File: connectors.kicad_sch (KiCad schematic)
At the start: 14 parts, among them J1 USB-C_DX07S024JJ2, J2 PCIe_x4_Conn_EdgeMount_NoMill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, J3 Molex_Nano-Fit-1053xx_xx02-ho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

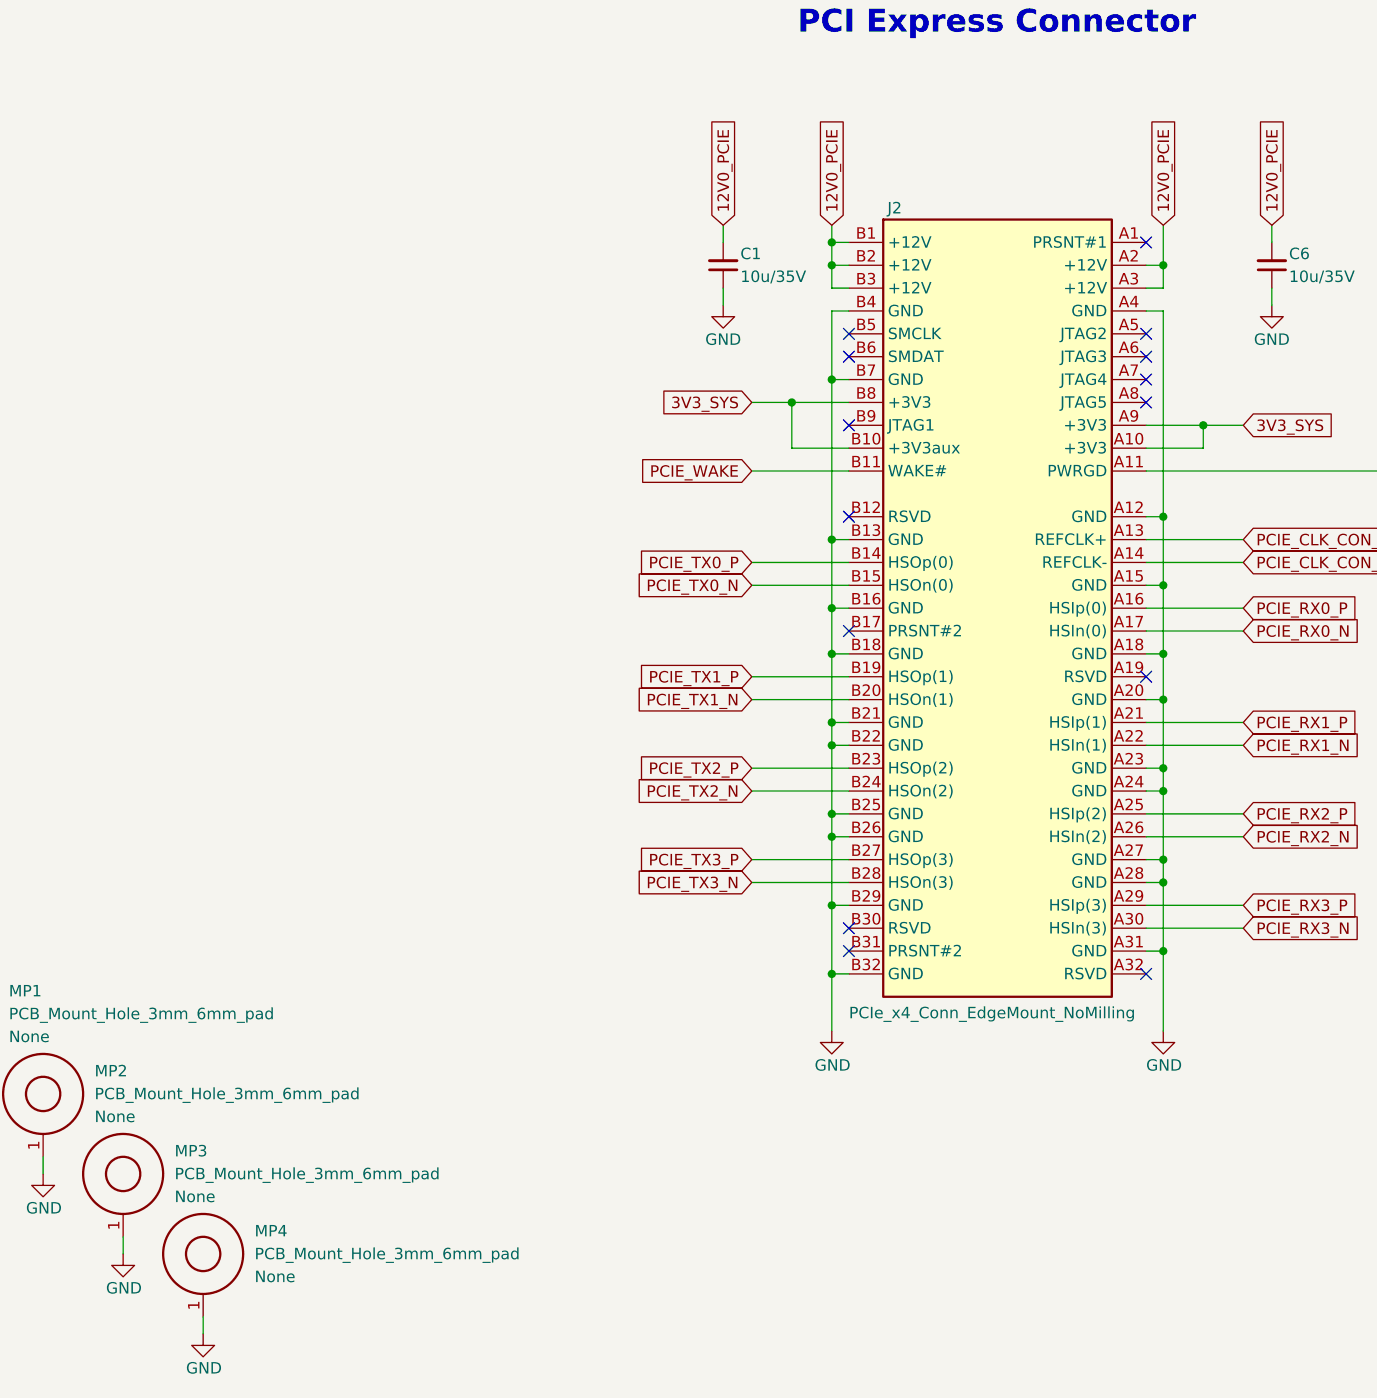
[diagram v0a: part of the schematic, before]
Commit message: Change PCIe connector, align nearby components and copper planes
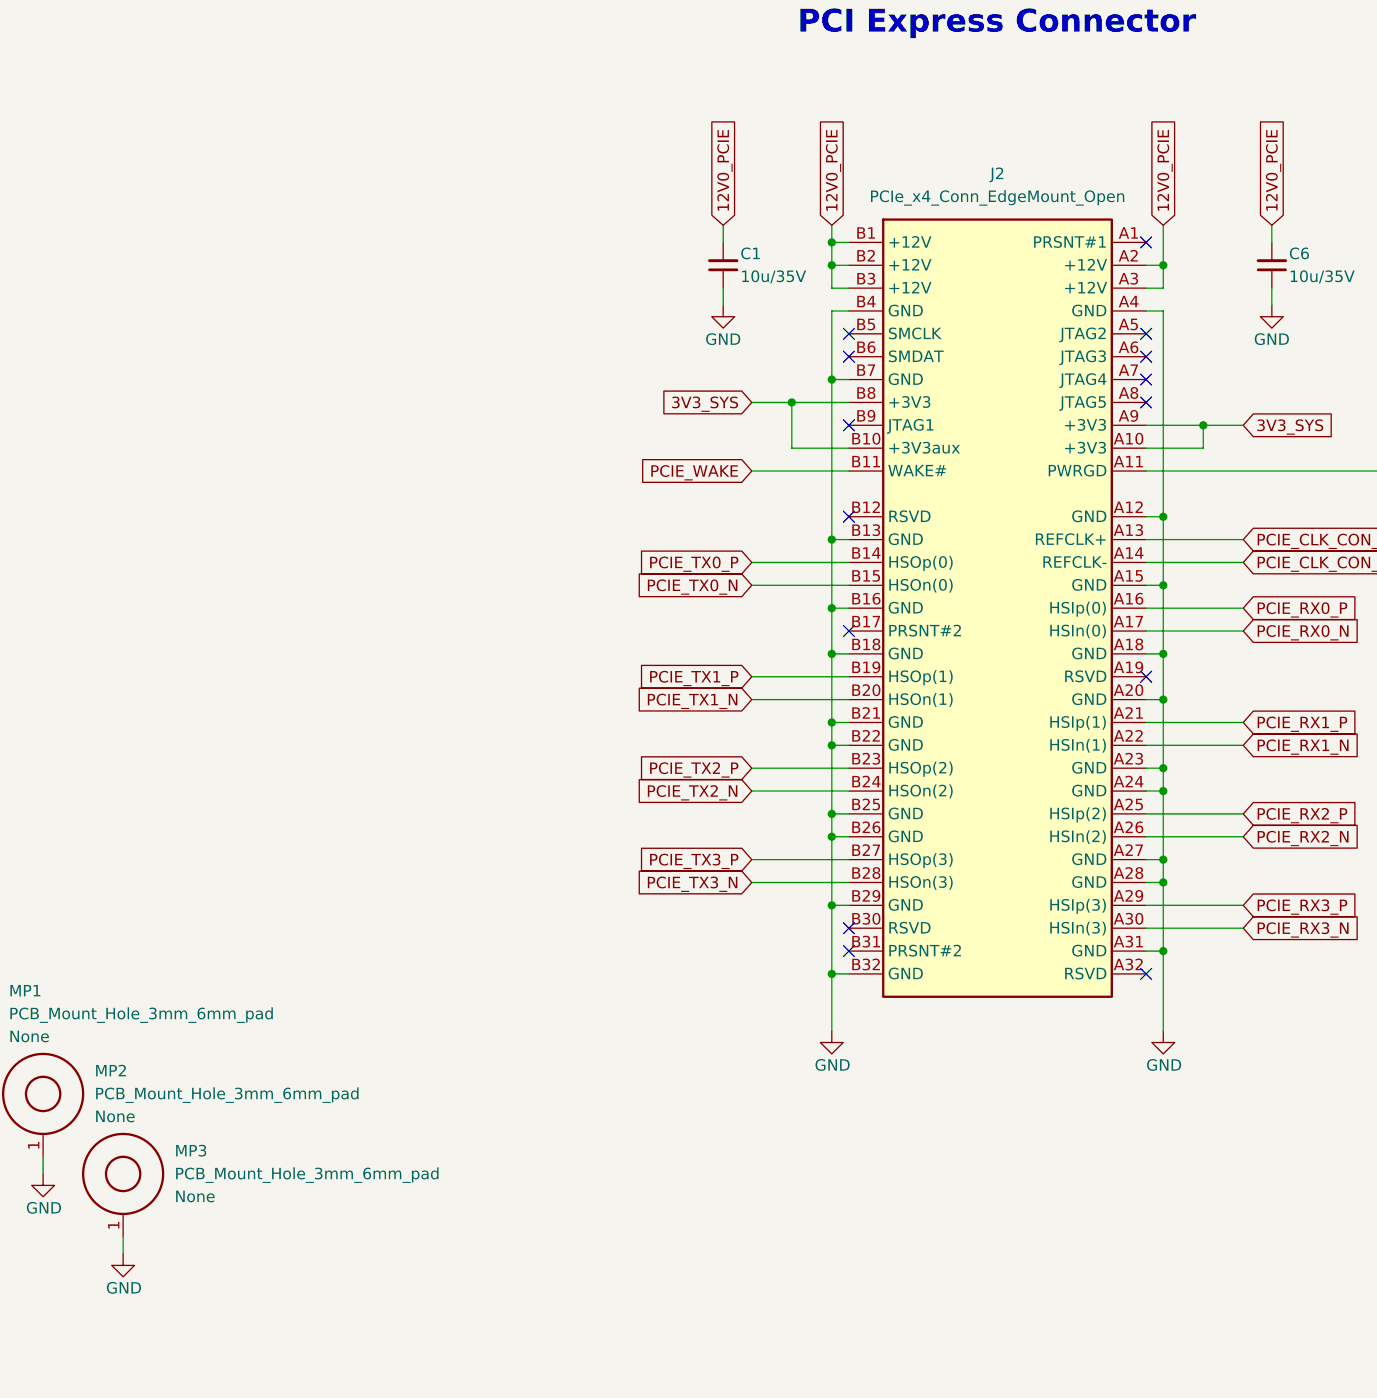
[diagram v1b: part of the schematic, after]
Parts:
- removed J2: PCIe_x4_Conn_EdgeMount_NoMilling, antmicro-footprints:PCIE_TE_6-1734857-5, symbol antmicroPciConnectors:PCIe_x4_Conn_EdgeMount_NoMilling
- removed MP4: PCB_Mount_Hole_3mm_6mm_pad, antmicro-footprints:mounting-hole-3.2mm, symbol antmicroMechanicalParts:PCB_Mount_Hole_3mm_6mm_pad
- added J2: PCIe_x4_Conn_EdgeMount_Open, antmicro-footprints:PCIE_TE_2-2387405-2, symbol antmicroPciConnectors:PCIe_x4_Conn_EdgeMount_Open
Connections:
- net 12V0_PCIE: now also J2.A2 (+12V), J2.A3 (+12V), J2.B1 (+12V), J2.B2 (+12V), J2.B3 (+12V)
- net 3V3_SYS: now also J2.A10 (+3V3), J2.A9 (+3V3), J2.B10 (+3V3aux), J2.B8 (+3V3)
- net GND: now also J2.A12 (GND), J2.A15 (GND), J2.A18 (GND), J2.A20 (GND), J2.A23 (GND), J2.A24 (GND), J2.A27 (GND), J2.A28 (GND), J2.A31 (GND), J2.A4 (GND), J2.B13 (GND), J2.B16 (GND), J2.B18 (GND), J2.B21 (GND), J2.B22 (GND), J2.B25 (GND), J2.B26 (GND), J2.B29 (GND), J2.B32 (GND), J2.B4 (GND), J2.B7 (GND)
- net PCIE_CLK_CON_N: now also J2.A14 (REFCLK-)
- net PCIE_CLK_CON_P: now also J2.A13 (REFCLK+)
- net PCIE_PWRGD: now also J2.A11 (PWRGD)
- net PCIE_RX0_N: now also J2.A17 (HSIn(0))
- net PCIE_RX0_P: now also J2.A16 (HSIp(0))
- net PCIE_RX1_N: now also J2.A22 (HSIn(1))
- net PCIE_RX1_P: now also J2.A21 (HSIp(1))
- net PCIE_RX2_N: now also J2.A26 (HSIn(2))
- net PCIE_RX2_P: now also J2.A25 (HSIp(2))
- net PCIE_RX3_N: now also J2.A30 (HSIn(3))
- net PCIE_RX3_P: now also J2.A29 (HSIp(3))
- net PCIE_TX0_N: now also J2.B15 (HSOn(0))
- net PCIE_TX0_P: now also J2.B14 (HSOp(0))
- net PCIE_TX1_N: now also J2.B20 (HSOn(1))
- net PCIE_TX1_P: now also J2.B19 (HSOp(1))
- net PCIE_TX2_N: now also J2.B24 (HSOn(2))
- net PCIE_TX2_P: now also J2.B23 (HSOp(2))
- net PCIE_TX3_N: now also J2.B28 (HSOn(3))
- net PCIE_TX3_P: now also J2.B27 (HSOp(3))
- net PCIE_WAKE: now also J2.B11 (WAKE#)

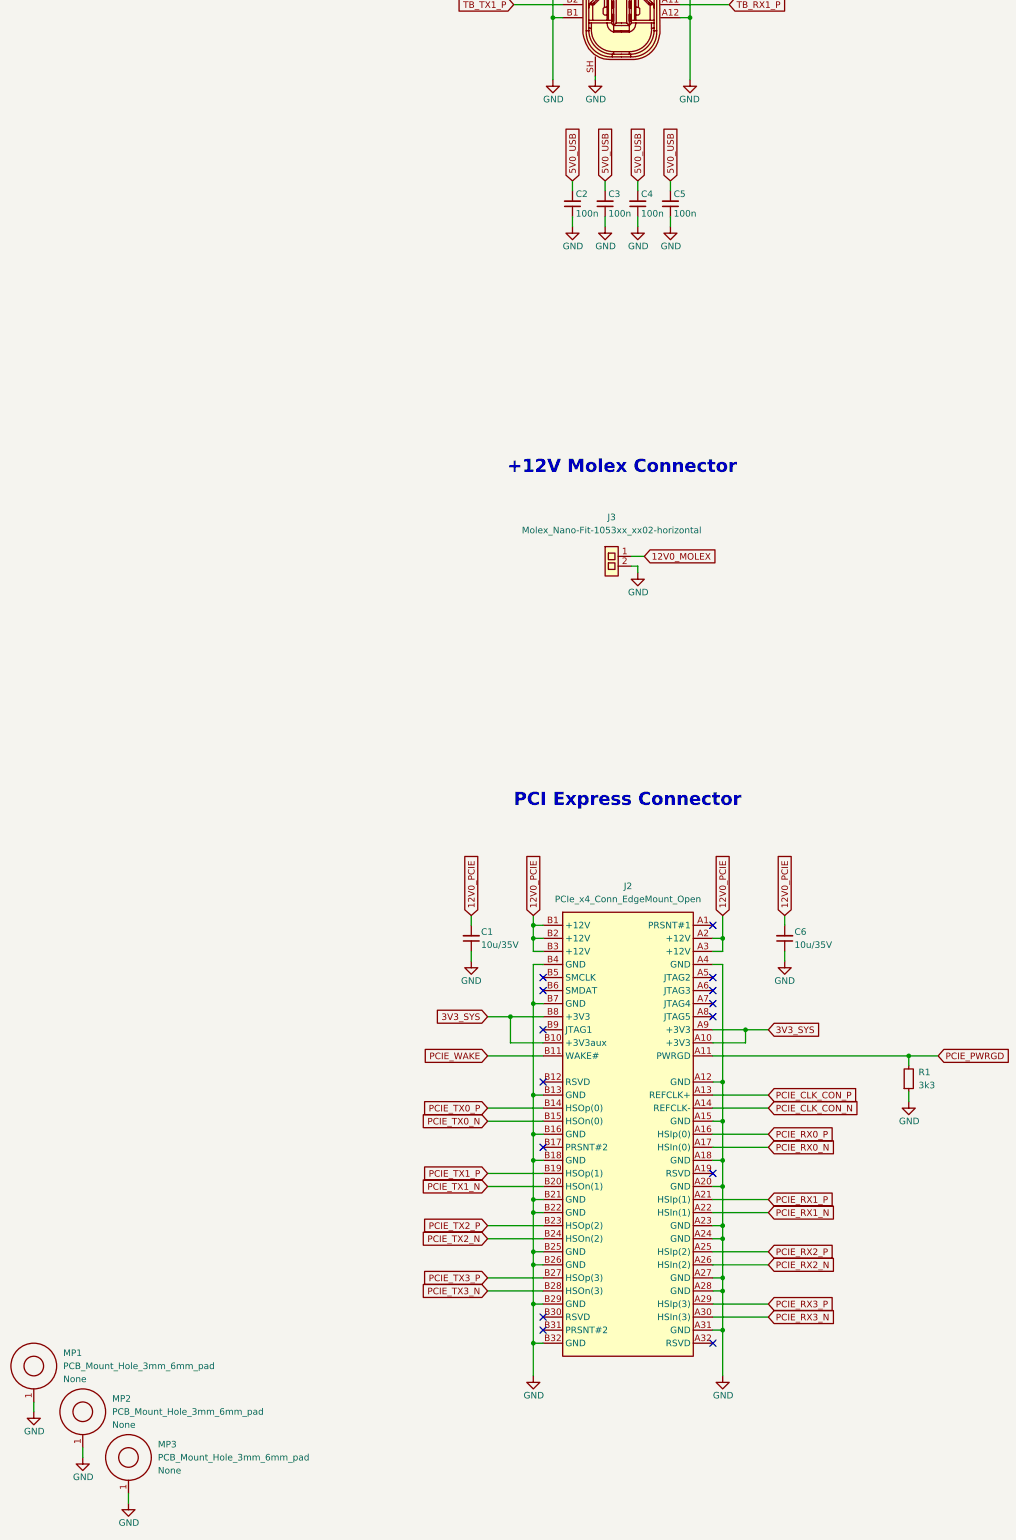
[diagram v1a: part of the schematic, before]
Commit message: Update all symbols from library to fix issues shown by klibs-check-license script
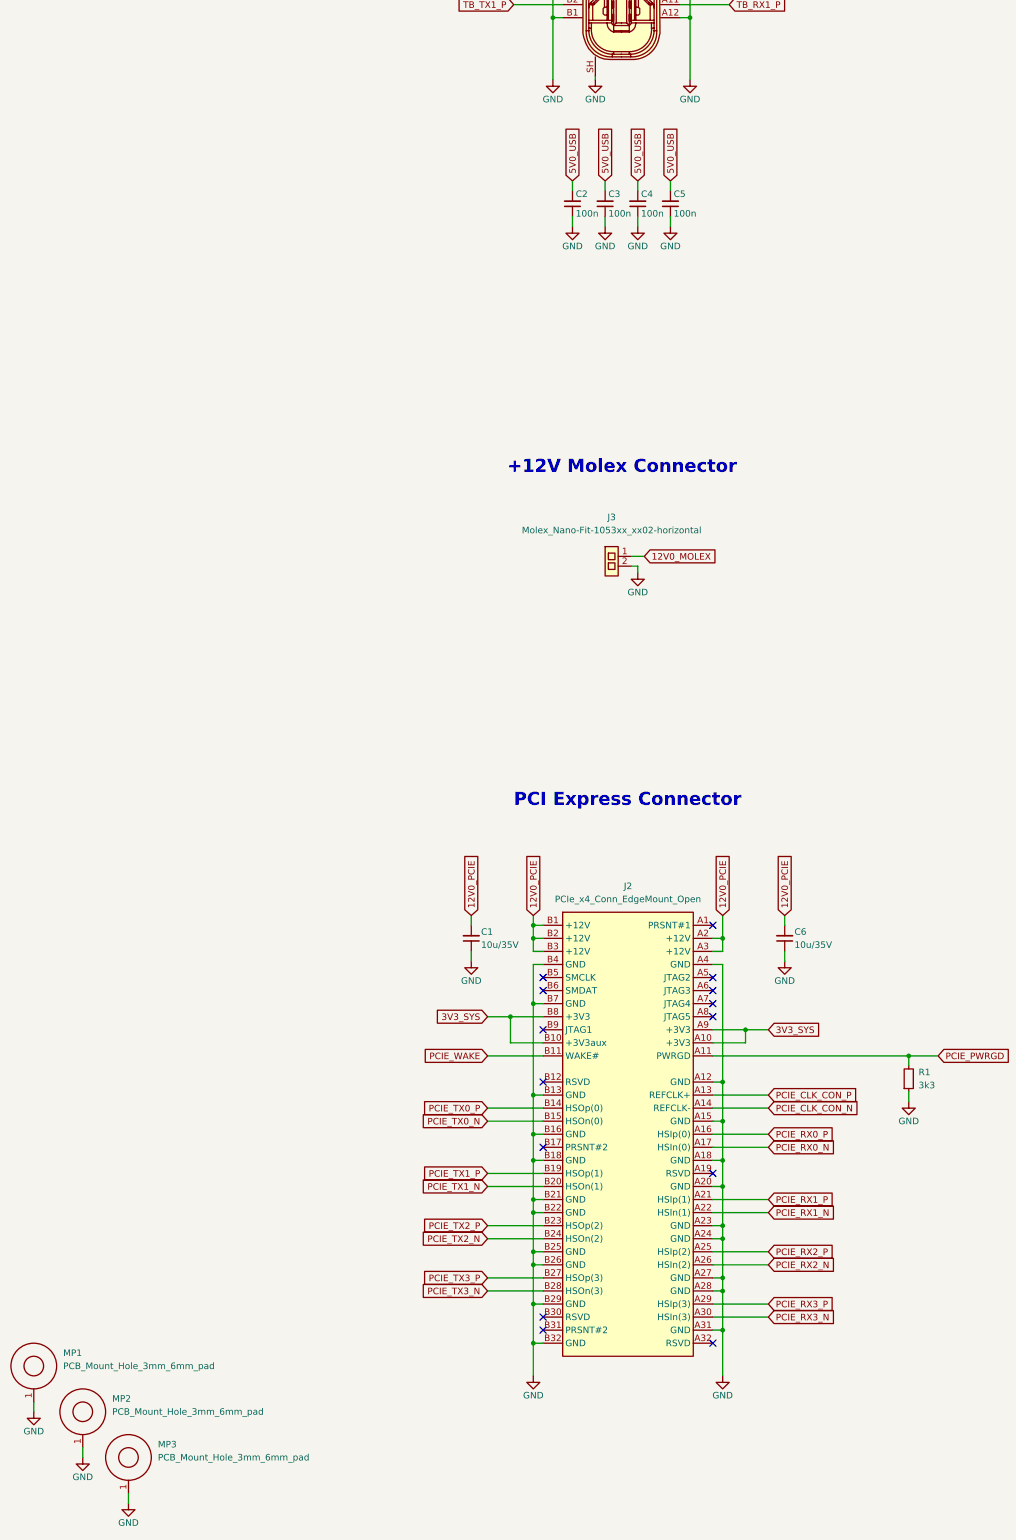
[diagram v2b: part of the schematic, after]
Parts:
- C1, C2, C3, C4, C5, C6, R1: Author (none) -> Antmicro; Copyright Copyright (c) 2023 Antmicro -> (none); License Apache-2.0 License -> Apache-2.0
- MP1, MP2, MP3: Manufacturer None -> (none)

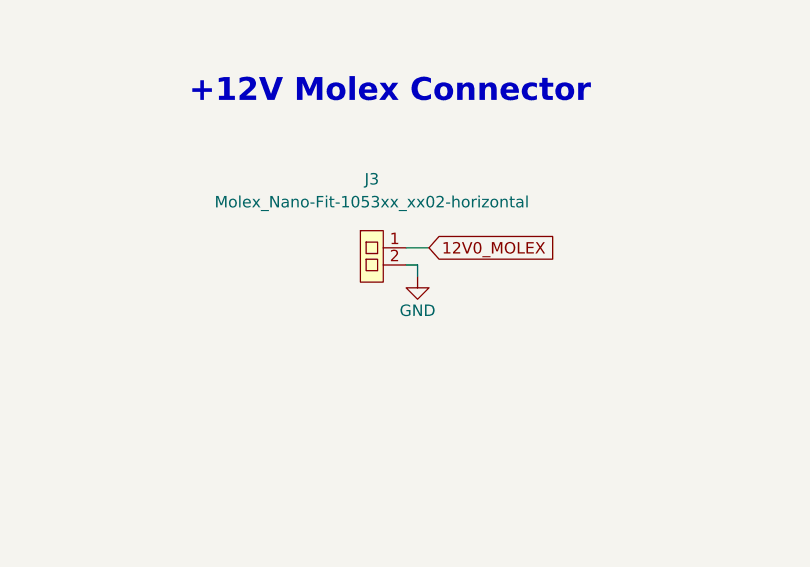
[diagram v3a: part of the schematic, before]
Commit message: Standardize all symbols on schematic
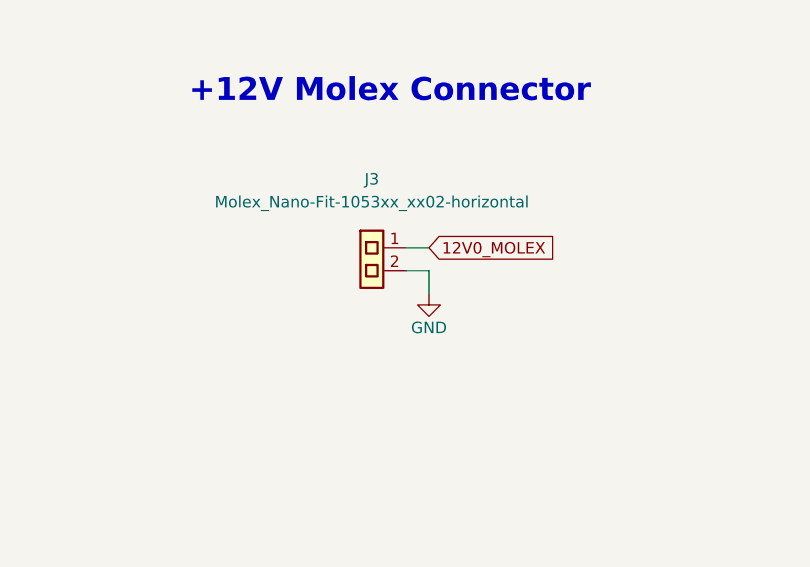
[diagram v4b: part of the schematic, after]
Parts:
- J3: Author (none) -> Antmicro; License (none) -> Apache-2.0
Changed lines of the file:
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@@
+    (stroke (width 0) (type default) (color 0 0 0 0))
+  )
+  (wire (pts (xy 154.305 197.485) (xy 154.305 194.945))
     (stroke (width 0) (type default) (color 0 0 0 0))
   )
@@
     (stroke (width 0) (type default) (color 0 0 0 0))
   )
+  (wire (pts (xy 154.305 194.945) (xy 151.765 194.945))
+    (stroke (width 0) (type default) (color 0 0 0 0))
+  )
   (wire (pts (xy 128.905 69.85) (xy 138.43 69.85))
     (stroke (width 0) (type default) (color 0 0 0 0))
@@
     (stroke (width 0) (type default) (color 0 0 0 0))
   )
-  (wire (pts (xy 151.765 194.31) (xy 153.035 194.31))
-    (stroke (width 0) (type default) (color 0 0 0 0))
-  )
   (wire (pts (xy 169.545 302.26) (xy 169.545 309.88))
-    (stroke (width 0) (type default) (color 0 0 0 0))
-  )
-  (wire (pts (xy 153.035 194.31) (xy 153.035 195.58))
     (stroke (width 0) (type default) (color 0 0 0 0))
   )
@@
     (pin "1")
   )
-  (symbol (lib_id "antmicroRectangularConnectorsHeadersFemalePins:Molex_Nano-Fit-1053xx_xx02-horizontal") (at 146.685 190.5 0) (unit 1)
+  (symbol (lib_id "antmicroRectangularConnectorsHeadersFemalePins:Molex_Nano-Fit-1053xx_xx02-horizontal") (at 151.765 192.405 0) (unit 1)
     (in_bom yes) (on_board yes) (fields_autoplaced)
     (property "Reference" "J3" (id 0) (at 147.955 184.785 0))
     (property "Value" "Molex_Nano-Fit-1053xx_xx02-horizontal" (id 1) (at 147.955 187.325 0))
-    (property "Footprint" "antmicro-footprints:Molex_Nano-Fit_1053xx-xx02_1x02_P2.50mm_Horizontal" (id 2) (at 142.24 198.755 0)
-      (effects (font (size 1.27 1.27)) hide)
-    )
-    (property "Datasheet" "https://www.molex.com/molex/products/part-detail/pcb_headers/1053131202" (id 3) (at 146.685 190.5 0)
-      (effects (font (size 1.27 1.27)) hide)
-    )
-    (property "Manufacturer" "Molex" (id 4) (at 145.415 203.835 0)
-      (effects (font (size 1.27 1.27)) hide)
-    )
-    (property "MPN" "1053131202" (id 5) (at 143.51 201.93 0)
-      (effects (font (size 1.27 1.27)) hide)
+    (property "Footprint" "antmicro-footprints:Molex_Nano-Fit_1053xx-xx02_1x02_P2.50mm_Horizontal" (id 2) (at 147.32 200.66 0)
+      (effects (font (size 1.27 1.27)) hide)
+    )
+    (property "Datasheet" "https://www.molex.com/molex/products/part-detail/pcb_headers/1053131202" (id 3) (at 151.765 192.405 0)
+      (effects (font (size 1.27 1.27)) hide)
+    )
+    (property "Manufacturer" "Molex" (id 4) (at 150.495 205.74 0)
+      (effects (font (size 1.27 1.27)) hide)
+    )
+    (property "MPN" "1053131202" (id 5) (at 148.59 203.835 0)
+      (effects (font (size 1.27 1.27)) hide)
+    )
+    (property "Author" "Antmicro" (id 6) (at 172.085 212.725 0)
+      (effects (font (size 1.27 1.27) (thickness 0.15)) (justify left bottom) hide)
+    )
+    (property "License" "Apache-2.0" (id 7) (at 172.085 215.265 0)
+      (effects (font (size 1.27 1.27) (thickness 0.15)) (justify left bottom) hide)
     )
     (pin "1")
@@
     (pin "1")
   )
-  (symbol (lib_id "antmicropower:GND") (at 153.035 195.58 0) (unit 1)
-    (in_bom yes) (on_board yes)
-    (property "Reference" "#PWR0146" (id 0) (at 153.035 201.93 0)
-      (effects (font (size 1.27 1.27)) hide)
-    )
-    (property "Value" "GND" (id 1) (at 153.035 199.39 0))
-    (property "Footprint" "" (id 2) (at 153.035 195.58 0)
-      (effects (font (size 1.27 1.27)) hide)
-    )
-    (property "Datasheet" "" (id 3) (at 153.035 195.58 0)
-      (effects (font (size 1.27 1.27)) hide)
-    )
+  (symbol (lib_id "antmicropower:GND") (at 154.305 197.485 0) (unit 1)
+    (in_bom yes) (on_board yes)
+    (property "Reference" "#PWR0146" (id 0) (at 154.305 203.835 0)
+      (effects (font (size 1.27 1.27)) hide)
+    )
+    (property "Value" "GND" (id 1) (at 154.305 201.295 0))
+    (property "Footprint" "" (id 2) (at 154.305 197.485 0)
+      (effects (font (size 1.27 1.27)) hide)
+    )
+    (property "Datasheet" "" (id 3) (at 154.305 197.485 0)
+      (effects (font (size 1.27 1.27)) hide)
+    )
